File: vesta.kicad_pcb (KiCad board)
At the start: 4 copper layers, 43 x 61.1 mm, 59 parts, among them J1 Solar Panel, J2 Solar Panel, J3 Conn_ARM_SWD_TagConnect_TC203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, J4 U.FL, U1 STM32WL55CCU6, U2 BQ24074RGTR, U3 TPS63900DSKR, U4 BME688_C3664478, U6 PE4259-63, X1 Q13FC1350000400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

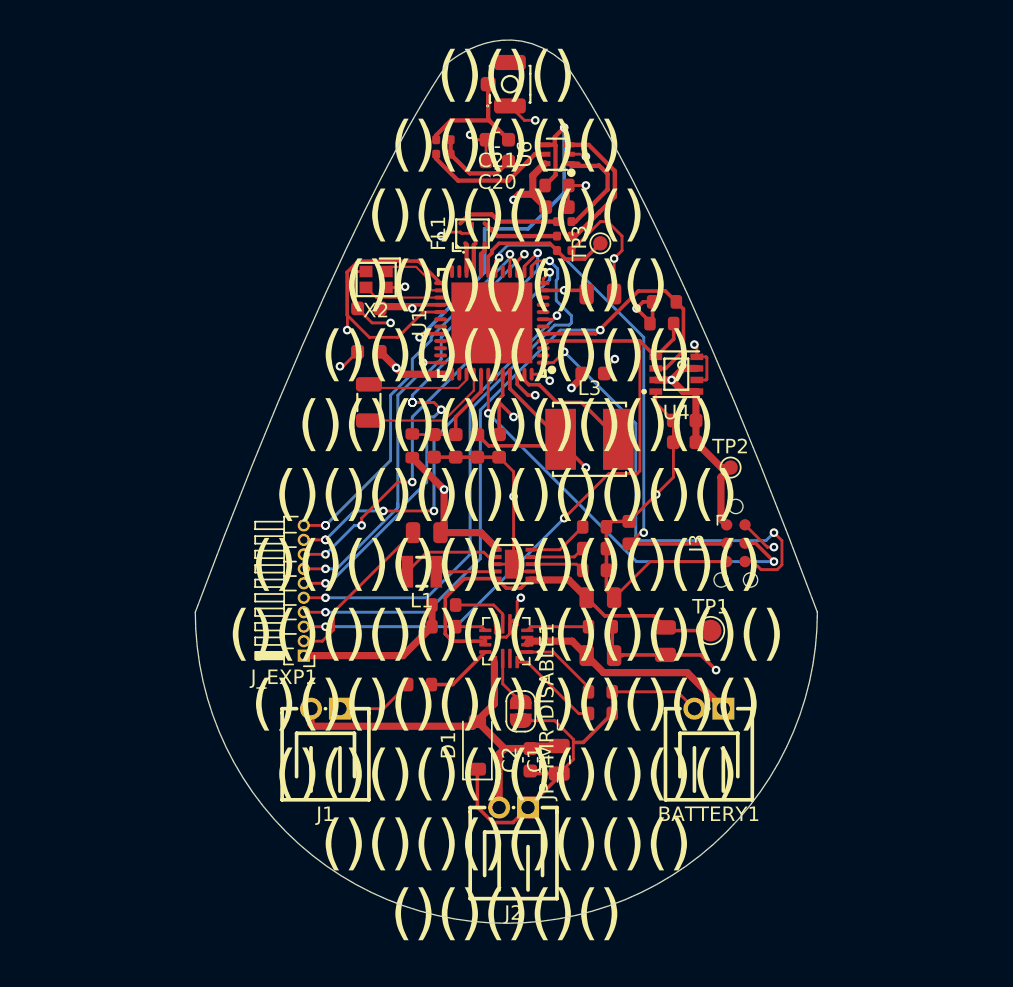
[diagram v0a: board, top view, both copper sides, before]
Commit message: feat: improving the thermal dissipation of the sensor
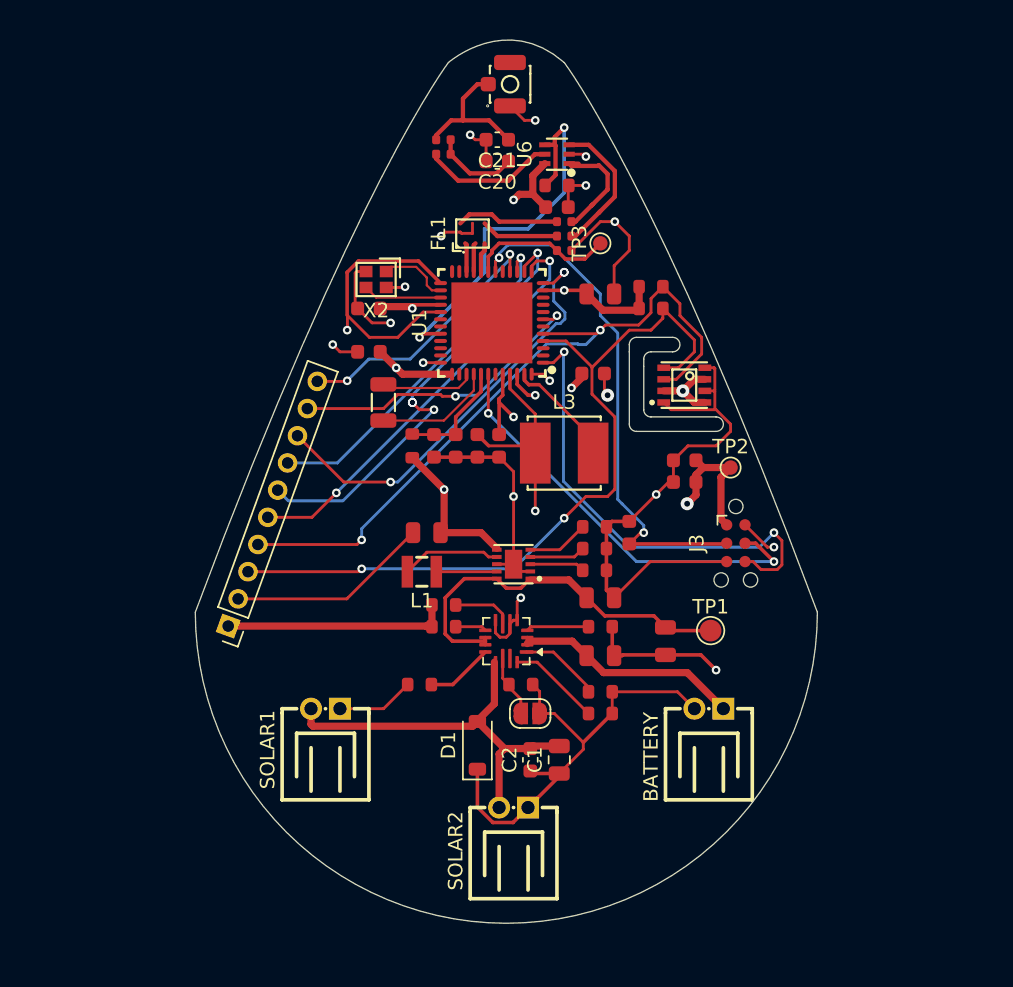
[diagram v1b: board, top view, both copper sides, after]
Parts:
- added R7: 68kΩ, PCM_JLCPCB:R_0603, F.Cu at (41.0, 62.5)
- J_EXP1: footprint Connector_PinHeader_1.00mm:PinHeader_1x10_P1.00mm_Horizontal -> Connector_PinHeader_2.00mm:PinHeader_1x10_P2.00mm_Vertical
- R1: value 8.0kΩ -> 7.87kΩ
- R2: value 8.87(or 8.9)kΩ -> 8.87kΩ
- moved J_EXP1 5.61 mm to (20.8, 58.5), turned to 160 degrees
- moved C22 2.75 mm to (52.3, 47.0)
- moved C23 2.75 mm to (52.3, 48.5)
- moved L3 1.99 mm to (44.0, 46.5)
- moved R15 1.40 mm to (50.0, 35.0)
- moved R16 1.29 mm to (50.0, 36.5)
- moved X1 1.00 mm to (31.5, 43.0)
- moved U4 0.93 mm to (52.3, 41.8)
- moved JP_TMR_DISABLE1 0.67 mm to (41.6, 64.5), turned to 0 degrees
- renumbered BATTERY1 to BATTERY, J1 to SOLAR1, J2 to SOLAR2
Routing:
- net /SPI1_SCK: track 39.0 -> 29.4 mm
- net /EXP_GPIO_CS1: track 26.7 -> 18.4 mm, vias 3 -> 2
- net GND: track 143.3 -> 151.7 mm, vias 16 -> 15
- net /SPI1_MOSI: track 31.4 -> 23.9 mm, vias 2 -> 1
- net /EXP_INT_WAKE: track 27.9 -> 21.1 mm, vias 5 -> 2
- net /I2C1_SCL: track 47.7 -> 54.4 mm
- net /3V3_SYS: track 72.2 -> 76.6 mm
- net /SPI1_MISO: track 35.1 -> 31.0 mm, vias 7 -> 6
- net /SMPS_1V55: track 55.0 -> 52.9 mm
- net /I2C1_SDA: track 51.3 -> 49.6 mm
- net Net-(J4-In): track 8.82 -> 9.96 mm
- net /SWO: track 31.8 -> 33.0 mm
- net /PC15-OSC32_OUT: track 9.24 -> 8.24 mm
- net /EXP_SPI_CS0: track 29.2 -> 30.1 mm, vias 4 -> 3
- net Net-(JP_TMR_DISABLE1-A): track 3.52 -> 4.32 mm
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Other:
- outline, holes or cut-outs redrawn
- board text removed: "()()() ()()()()() ()()()()()() ()()()()()()() ()()()()()()()() ()()()()()()()()() ()()()()()()()()()() ()()()()()()()()()()() ()()()()()()()()()()()() ()()()()()()()()()()() ()()()()()()()()()() ()()()()()()()() ()()()()()"

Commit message: feat: updating the footprint of the antenna
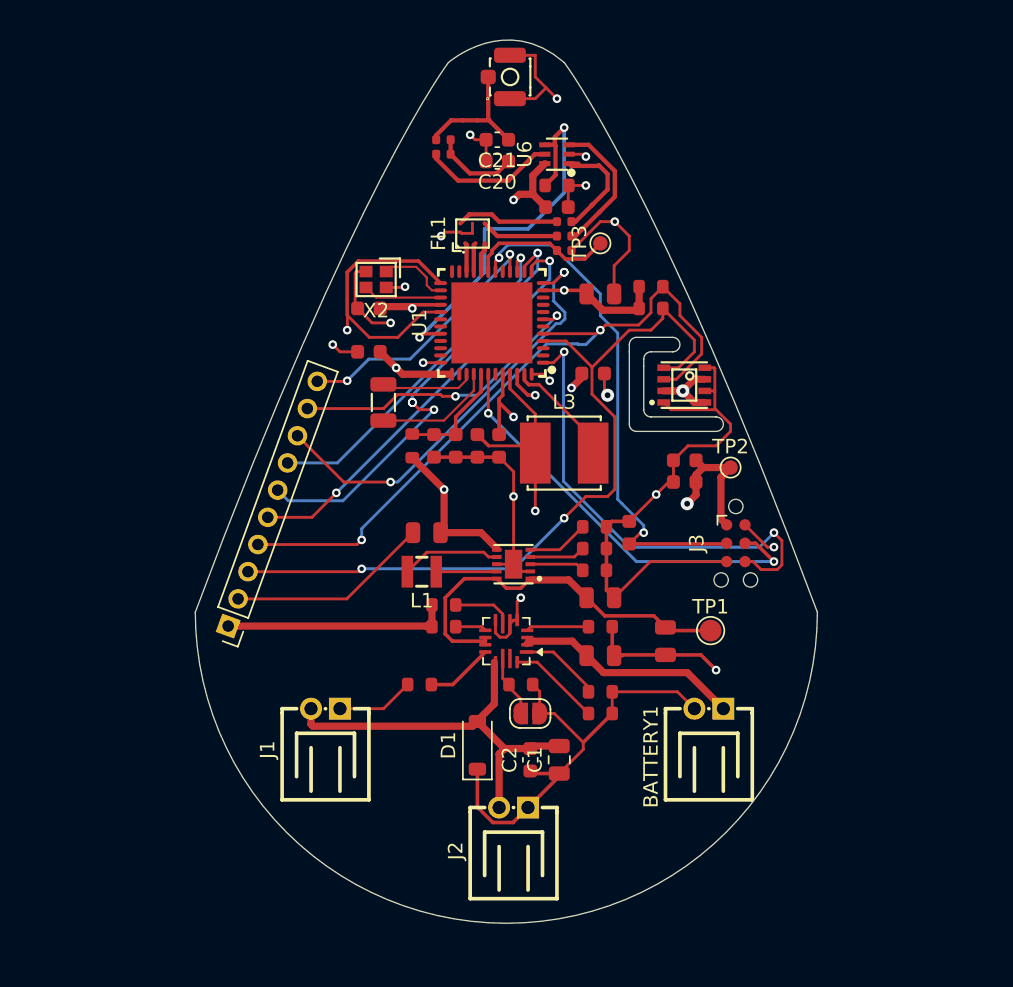
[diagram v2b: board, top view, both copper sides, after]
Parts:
- removed J4: U.FL, PCM_JLCPCB:IPEX-SMD_BWIPX-1-001E
- added U.FL1: Conn_01x03, PCM_JLCPCB:IPEX-SMD_BWIPX-1-001E, F.Cu at (39.5, 20.5)
- renumbered BATTERY to BATTERY1, SOLAR1 to J1, SOLAR2 to J2
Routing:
- net GND: track 151.7 -> 157.7 mm
- net Net-(U.FL1-Pin_1): track 9.96 -> 9.32 mm

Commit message: feat: updating the references and adding the logo
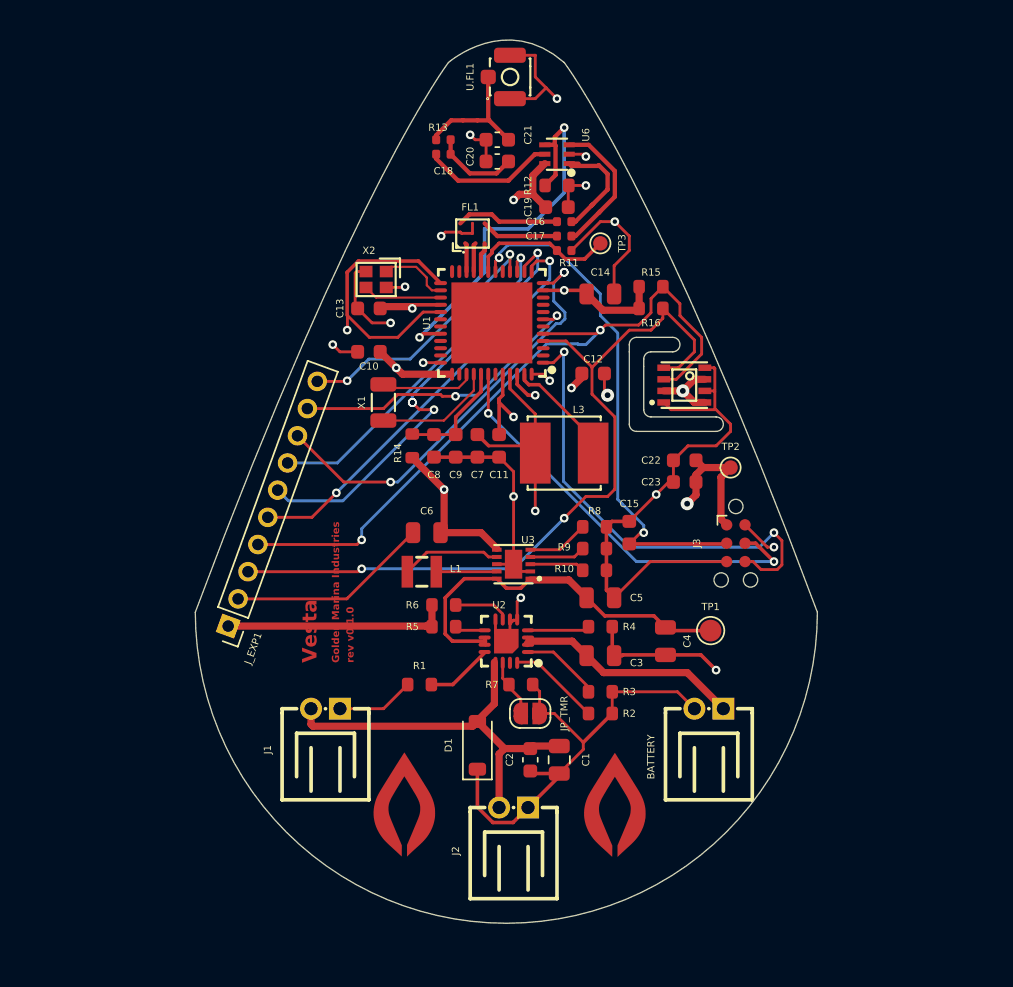
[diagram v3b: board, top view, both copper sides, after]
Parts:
- added G***: LOGO, Logo:logo, F.Cu at (33.0, 74.5)
- added G***: LOGO, Logo:logo, F.Cu at (47.6, 74.5)
- U2: footprint Package_DFN_QFN:MPS_QFN-16_3x3mm_P0.5mm -> JLCImport:BQ24074RGTR
- renumbered BATTERY1 to BATTERY, JP_TMR_DISABLE1 to JP_TMR
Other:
- board text added: "Golden Marina Industries"
- board text added: "Vesta"
- board text added: "rev v0.1.0"

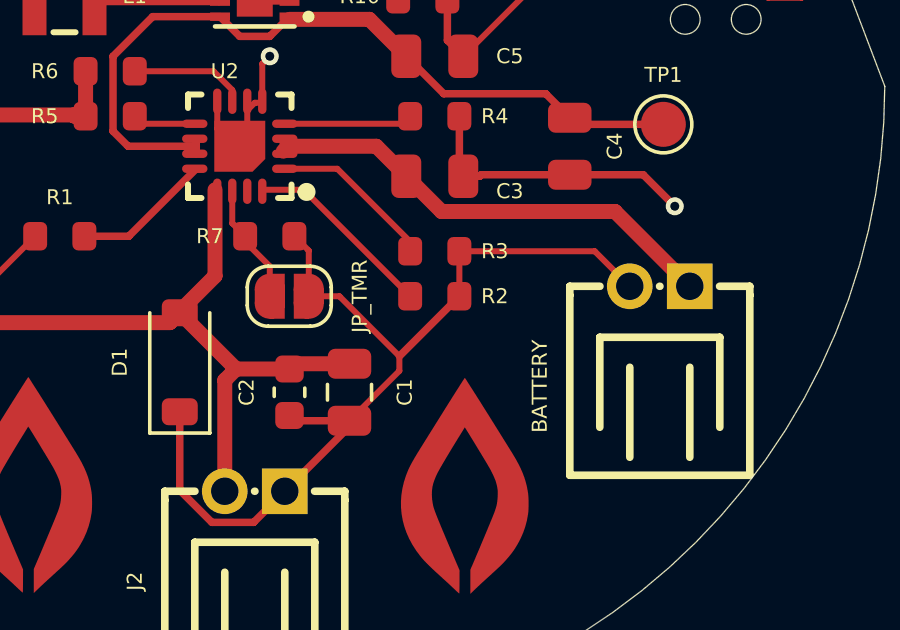
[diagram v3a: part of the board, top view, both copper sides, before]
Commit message: feat: updating footprints
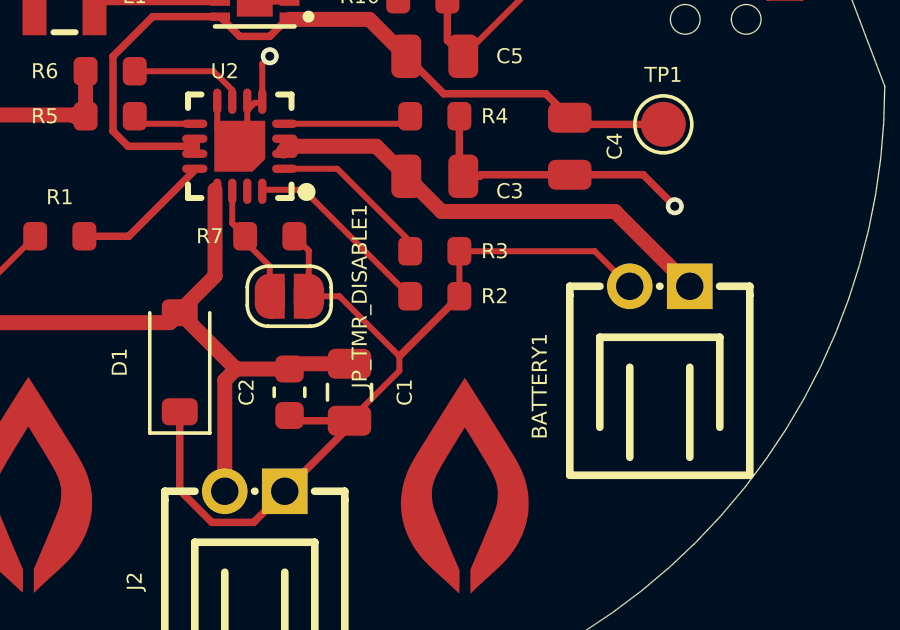
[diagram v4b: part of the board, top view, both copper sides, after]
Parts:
- renumbered BATTERY to BATTERY1, JP_TMR to JP_TMR_DISABLE1
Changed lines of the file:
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@@
 		(descr "-25℃~+85℃ 1 1x2P 2 250V 2A 2P 2mm 4.7mm 6.05mm 6mm Brass PA66 PH Right Angle Tin UL94V-0 White 弯插,P=2mm Wire To Board Connector ROHS")
 		(tags "C5359610 CONN-TH_2P-P2.00_GP01-2001WR-2P WAFER-PH2.0-2PWZ XUNPU")
-		(property "Reference" "BATTERY"
+		(property "Reference" "BATTERY1"
 			(at 4 -3.332474 90)
 			(layer "F.SilkS")
@@
 		(descr "SMD Solder Jumper, 1x1.5mm, rounded Pads, 0.3mm gap, open")
 		(tags "solder jumper open")
-		(property "Reference" "JP_TMR"
+		(property "Reference" "JP_TMR_DISABLE1"
 			(at 2.35 0 90)
 			(layer "F.SilkS")
